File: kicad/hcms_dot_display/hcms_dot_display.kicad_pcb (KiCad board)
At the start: 2 copper layers, 35.5 x 39.9 mm, 45 parts, among them J1 Conn_01x12, J2 USB_C_Receptacle_USB2.0, J3 Conn_01x12, J4 Conn_01x10_Female, J5 Conn_01x10_Male, J6 Conn_01x10_Male, J7 Conn_01x10_Female, Q1 Q_PMOS_DSG, Q2 Q_PMOS_DSG, Q3 Q_PMOS_DSG, Q4 Q_PMOS_DSG, Q5 Q_PMOS_DSG, Q6 Q_PMOS_DSG, SW2 SW_SPST, U1 ATtiny826-SXX, U2 FT231XS

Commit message: beginning of ecos
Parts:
- added R16: DNP, Resistor_SMD:R_0603_1608Metric, F.Cu at (202.3, 120.5)
- added R17: DNP, Resistor_SMD:R_0603_1608Metric, F.Cu at (206.4, 120.5)
- C1, C2, C7, C8, C9, R15, U2: moved to F.Cu
- C12, Q6, R3, U1: moved to B.Cu
- J1, J3: footprint hcms:input board to board con top bot -> hcms:board to board con top bot
- J4: value Conn_01x10_Female -> Conn_01x11_Female; footprint Connector_PinHeader_2.54mm:PinHeader_1x10_P2.54mm_Vertical -> Connector_PinSocket_2.54mm:PinSocket_1x11_P2.54mm_Vertical
- J5: value Conn_01x10_Male -> Conn_01x11_Male; footprint Connector_PinHeader_2.54mm:PinHeader_1x10_P2.54mm_Vertical -> Connector_PinHeader_2.54mm:PinHeader_1x11_P2.54mm_Vertical
- J6: value Conn_01x10_Male -> Conn_01x12; footprint Connector_PinHeader_2.54mm:PinHeader_1x10_P2.54mm_Vertical -> hcms:board to board con left right
- J7: value Conn_01x10_Female -> Conn_01x12; footprint Connector_PinHeader_2.54mm:PinHeader_1x10_P2.54mm_Vertical -> hcms:board to board con left right
- moved J7 46.7 mm to (164.1, 99.6)
- moved Q6 42.6 mm to (180.9, 122.8), turned to -90 degrees
- moved C12 36.9 mm to (175.6, 121.0), turned to 180 degrees
- moved R3 36.7 mm to (182.4, 117.0), turned to 180 degrees
- moved U1 33.0 mm to (191.2, 123.0), turned to -90 degrees
- moved J5 25.8 mm to (167.8, 114.3), turned to 90 degrees
- moved R2 20.3 mm to (189.8, 99.8)
- moved R1 20.3 mm to (191.4, 99.8)
- moved J6 20.0 mm to (196.9, 99.6)
- moved J3 18.6 mm to (180.5, 108.3)
- moved J1 18.5 mm to (180.5, 91.2)
- moved SW2 14.7 mm to (193.3, 123.9)
- moved R6 14.4 mm to (181.3, 99.8)
- moved R7 14.4 mm to (179.8, 99.8)
- moved C2 10.2 mm to (186.1, 122.3), turned to 0 degrees
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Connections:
- J3 pad 10: /DAISY_A_DATA -> /A_DATA
- J3 pad 11: /DAISY_B_DATA -> /B_DATA
- J4 pad 10: GND -> /MCU_DATA
- J4 pad 2: /MCU_COL_1 -> /V_COL
- J4 pad 3: /MCU_COL_2 -> /MCU_COL_1
- J4 pad 4: /MCU_COL_3 -> /MCU_COL_2
- J4 pad 5: /MCU_COL_4 -> /MCU_COL_3
- J4 pad 6: /MCU_COL_5 -> /MCU_COL_4
- J4 pad 7: /nBLNK -> /MCU_COL_5
- J4 pad 8: /CLK -> /nBLNK
- J4 pad 9: /MCU_DATA -> /CLK
- J5 pad 10: GND -> /MCU_DATA
- J5 pad 2: /MCU_COL_1 -> /V_COL
- J5 pad 3: /MCU_COL_2 -> /MCU_COL_1
- J5 pad 4: /MCU_COL_3 -> /MCU_COL_2
- J5 pad 5: /MCU_COL_4 -> /MCU_COL_3
- J5 pad 6: /MCU_COL_5 -> /MCU_COL_4
- J5 pad 7: /nBLNK -> /MCU_COL_5
- J5 pad 8: /CLK -> /nBLNK
- J5 pad 9: /MCU_DATA -> /CLK
- J6 pad 10: GND -> /DAISY_A_DATA
- J6 pad 2: /MCU_COL_1 -> /V_COL
- J6 pad 3: /MCU_COL_2 -> /MCU_COL_1
- J6 pad 4: /MCU_COL_3 -> /MCU_COL_2
- J6 pad 5: /MCU_COL_4 -> /MCU_COL_3
- J6 pad 6: /MCU_COL_5 -> /MCU_COL_4
- J6 pad 7: /nBLNK -> /MCU_COL_5
- J6 pad 8: /CLK -> /nBLNK
- J6 pad 9: /MCU_DATA -> /CLK
- J7 pad 10: GND -> /A_DATA
- J7 pad 2: /MCU_COL_1 -> /V_COL
- J7 pad 3: /MCU_COL_2 -> /MCU_COL_1
- J7 pad 4: /MCU_COL_3 -> /MCU_COL_2
- J7 pad 5: /MCU_COL_4 -> /MCU_COL_3
- J7 pad 6: /MCU_COL_5 -> /MCU_COL_4
- J7 pad 7: /nBLNK -> /MCU_COL_5
- J7 pad 8: /CLK -> /nBLNK
- J7 pad 9: /MCU_DATA -> /CLK

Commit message: aidan im pushing
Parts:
- R16, R17: moved to B.Cu
- moved R17 37.7 mm to (176.9, 97.0), turned to 180 degrees
- moved R16 28.2 mm to (187.0, 97.0)
- moved C10 6.89 mm to (167.3, 97.1)

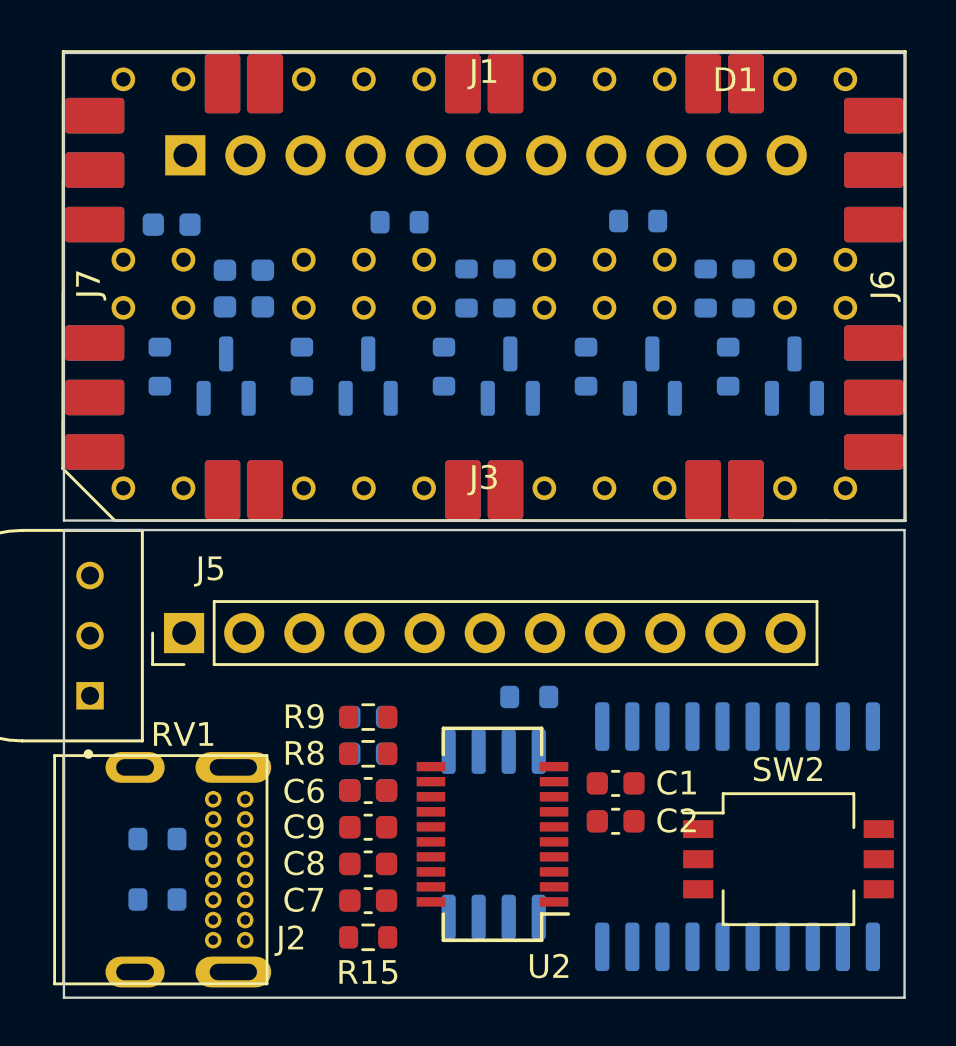
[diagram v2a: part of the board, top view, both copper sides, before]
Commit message: added switch fp, cleaned up placement. ready for routing
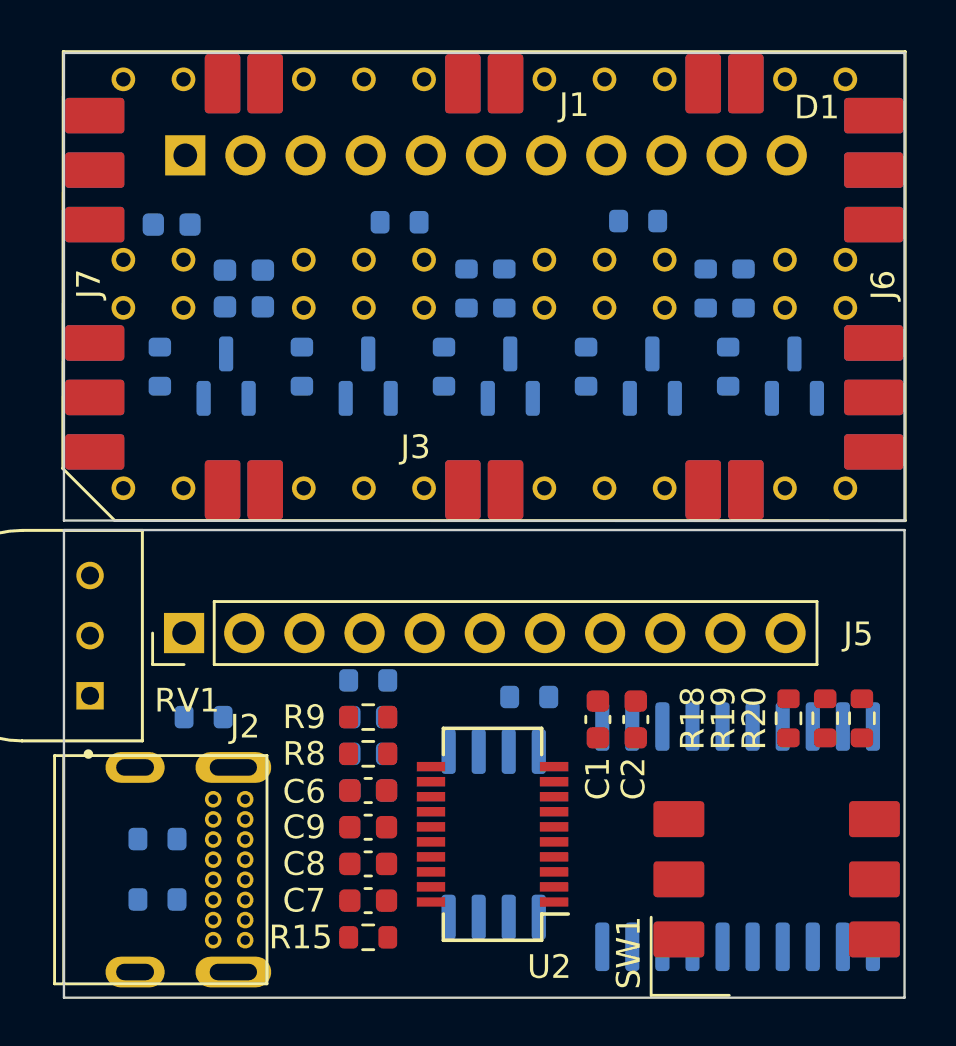
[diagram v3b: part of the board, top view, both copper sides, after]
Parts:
- removed SW2: SW_SPST, Button_Switch_SMD:SW_DIP_SPSTx03_Slide_KingTek_DSHP03TS_W7.62mm_P1.27mm
- added R18: 10k, Resistor_SMD:R_0603_1608Metric, F.Cu at (193.3, 118.0)
- added R19: 10k, Resistor_SMD:R_0603_1608Metric, F.Cu at (194.9, 118.0)
- added R20: 10k, Resistor_SMD:R_0603_1608Metric, F.Cu at (196.4, 118.0)
- added R21: 0, Resistor_SMD:R_0603_1608Metric, B.Cu at (168.7, 117.9)
- added R22: 0, Resistor_SMD:R_0603_1608Metric, B.Cu at (175.6, 116.3)
- added SW1: SW_DIP_x03, hcms:BPA03SB, F.Cu at (192.8, 124.8)
- R4, R5: value 10k -> 5.1k
- moved C2 4.38 mm to (186.9, 118.0), turned to 90 degrees
- moved C1 2.80 mm to (185.3, 118.0), turned to 90 degrees
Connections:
- C12 pad 1: /V_COL -> Net-(C12-Pad1)
- Q6 pad 1: /V_COL -> Net-(C12-Pad1)
- U1 pad 17: unconnected-(U1-Pad17) -> /CONFIG_0
- U1 pad 2: unconnected-(U1-Pad2) -> /CONFIG_1
- U1 pad 4: unconnected-(U1-Pad4) -> /CONFIG_2

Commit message: finally gonna start routing ??
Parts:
- moved C10 0.18 mm to (167.2, 97.0)
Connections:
- J4 pad 3: /MCU_COL_1 -> /MCU_COL_2
- J4 pad 4: /MCU_COL_2 -> /MCU_COL_4
- J4 pad 5: /MCU_COL_3 -> /MCU_COL_1
- J4 pad 6: /MCU_COL_4 -> /MCU_COL_3
- J5 pad 3: /MCU_COL_1 -> /MCU_COL_2
- J5 pad 4: /MCU_COL_2 -> /MCU_COL_4
- J5 pad 5: /MCU_COL_3 -> /MCU_COL_1
- J5 pad 6: /MCU_COL_4 -> /MCU_COL_3
- Q6 pad 1: Net-(C12-Pad1) -> +5V
- Q6 pad 3: Net-(Q6-Pad3) -> +5V
- Q6 pad 4: (no net) -> Net-(Q6-Pad4)
- Q6 pad 5: (no net) -> Net-(C12-Pad1)
- Q6 pad 6: (no net) -> Net-(C12-Pad1)
- Q6 pad 7: (no net) -> Net-(C12-Pad1)
- Q6 pad 8: (no net) -> Net-(C12-Pad1)
- R3 pad 2: Net-(Q6-Pad3) -> Net-(Q6-Pad4)
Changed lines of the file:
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@@
   (net 11 "/CLK")
   (net 12 "GND")
-  (net 13 "Net-(Q6-Pad3)")
+  (net 13 "Net-(Q6-Pad4)")
   (net 14 "+5V")
   (net 15 "Net-(J2-PadA5)")
@@
       (net 10 "/nBLNK") (pinfunction "nVB_13-16") (pintype "input"))
     (pad "15B" thru_hole circle locked (at 12.7 -8.635) (size 1 1) (drill 0.61) (layers *.Cu *.Mask)
-      (net 10 "/nBLNK") (pinfunction "nVB_13-16") (pintype "input"))
+      (net 10 "/nBLNK") (pinfunction "nVB_5-8") (pintype "input"))
     (pad "17A" thru_hole circle locked (at 7.62 1.015) (size 1 1) (drill 0.61) (layers *.Cu *.Mask)
       (net 11 "/CLK") (pinfunction "CLK") (pintype "input"))
@@
       (net 10 "/nBLNK") (pinfunction "nVB_9-12") (pintype "input"))
     (pad "22B" thru_hole circle locked (at -5.08 -8.635) (size 1 1) (drill 0.61) (layers *.Cu *.Mask)
-      (net 10 "/nBLNK") (pinfunction "nVB_9-12") (pintype "input"))
+      (net 10 "/nBLNK") (pinfunction "nVB_1-4") (pintype "input"))
     (pad "23A" thru_hole circle locked (at -7.62 1.015) (size 1 1) (drill 0.61) (layers *.Cu *.Mask)
       (net 14 "+5V") (pinfunction "VDD") (pintype "power_in"))
@@
       (net 6 "/V_COL") (pinfunction "Pin_2") (pintype "passive"))
     (pad "3" thru_hole oval locked (at 0 5.08 90) (size 1.7 1.7) (drill 1) (layers *.Cu *.Mask)
-      (net 28 "/MCU_COL_1") (pinfunction "Pin_3") (pintype "passive"))
+      (net 29 "/MCU_COL_2") (pinfunction "Pin_3") (pintype "passive"))
     (pad "4" thru_hole oval locked (at 0 7.62 90) (size 1.7 1.7) (drill 1) (layers *.Cu *.Mask)
-      (net 29 "/MCU_COL_2") (pinfunction "Pin_4") (pintype "passive"))
+      (net 21 "/MCU_COL_4") (pinfunction "Pin_4") (pintype "passive"))
     (pad "5" thru_hole oval locked (at 0 10.16 90) (size 1.7 1.7) (drill 1) (layers *.Cu *.Mask)
-      (net 30 "/MCU_COL_3") (pinfunction "Pin_5") (pintype "passive"))
+      (net 28 "/MCU_COL_1") (pinfunction "Pin_5") (pintype "passive"))
     (pad "6" thru_hole oval locked (at 0 12.7 90) (size 1.7 1.7) (drill 1) (layers *.Cu *.Mask)
-      (net 21 "/MCU_COL_4") (pinfunction "Pin_6") (pintype "passive"))
+      (net 30 "/MCU_COL_3") (pinfunction "Pin_6") (pintype "passive"))
     (pad "7" thru_hole oval locked (at 0 15.24 90) (size 1.7 1.7) (drill 1) (layers *.Cu *.Mask)
       (net 22 "/MCU_COL_5") (pinfunction "Pin_7") (pintype "passive"))
@@
       (net 6 "/V_COL") (pinfunction "Pin_2") (pintype "passive"))
     (pad "3" thru_hole oval locked (at 0 -5.08 270) (size 1.7 1.7) (drill 1) (layers *.Cu *.Mask)
-      (net 28 "/MCU_COL_1") (pinfunction "Pin_3") (pintype "passive"))
+      (net 29 "/MCU_COL_2") (pinfunction "Pin_3") (pintype "passive"))
     (pad "4" thru_hole oval locked (at 0 -7.62 270) (size 1.7 1.7) (drill 1) (layers *.Cu *.Mask)
-      (net 29 "/MCU_COL_2") (pinfunction "Pin_4") (pintype "passive"))
+      (net 21 "/MCU_COL_4") (pinfunction "Pin_4") (pintype "passive"))
     (pad "5" thru_hole oval locked (at 0 -10.16 270) (size 1.7 1.7) (drill 1) (layers *.Cu *.Mask)
-      (net 30 "/MCU_COL_3") (pinfunction "Pin_5") (pintype "passive"))
+      (net 28 "/MCU_COL_1") (pinfunction "Pin_5") (pintype "passive"))
     (pad "6" thru_hole oval locked (at 0 -12.7 270) (size 1.7 1.7) (drill 1) (layers *.Cu *.Mask)
-      (net 21 "/MCU_COL_4") (pinfunction "Pin_6") (pintype "passive"))
+      (net 30 "/MCU_COL_3") (pinfunction "Pin_6") (pintype "passive"))
     (pad "7" thru_hole oval locked (at 0 -15.24 270) (size 1.7 1.7) (drill 1) (layers *.Cu *.Mask)
       (net 22 "/MCU_COL_5") (pinfunction "Pin_7") (pintype "passive"))
@@
   )
   (footprint "Capacitor_SMD:C_0603_1608Metric" (layer "B.Cu")
-    (at 167.3 97.1 180)
+    (at 167.2 96.95 180)
     (descr "Capacitor SMD 0603 (1608 Metric), square (rectangular) end terminal, IPC_7351 nominal, (Body size source: IPC-SM-782 page 76, https://www.pcb-3d.com/wordpress/wp-content/uploads/ipc-sm-782a_amendment_1_and_2.pdf), generated with kicad-footprint-generator")
     (tags "capacitor")
@@
     (property "Sheetname" "")
     (attr smd)
-    (fp_text reference "C10" (at 3.4 0.05) (layer "B.SilkS")
+    (fp_text reference "C10" (at 0.65 -2.35 90) (layer "B.SilkS")
       (effects (font (size 1 1) (thickness 0.15)) (justify mirror))
     )
@@
     (fp_line (start 1.92 -1.7) (end 1.92 1.7) (layer "B.CrtYd") (width 0.05))
     (fp_line (start -1.92 -1.7) (end 1.92 -1.7) (layer "B.CrtYd") (width 0.05))
+    (fp_line (start 0.65 1.45) (end 0.65 -1.45) (layer "B.Fab") (width 0.1))
     (fp_line (start 0.65 -1.45) (end -0.65 -1.45) (layer "B.Fab") (width 0.1))
     (fp_line (start -0.65 1.125) (end -0.325 1.45) (layer "B.Fab") (width 0.1))
     (fp_line (start -0.325 1.45) (end 0.65 1.45) (layer "B.Fab") (width 0.1))
     (fp_line (start -0.65 -1.45) (end -0.65 1.125) (layer "B.Fab") (width 0.1))
-    (fp_line (start 0.65 1.45) (end 0.65 -1.45) (layer "B.Fab") (width 0.1))
     (pad "1" smd roundrect (at -0.9375 0.95 90) (size 1.475 0.6) (layers "B.Cu" "B.Paste" "B.Mask") (roundrect_rratio 0.25)
       (net 2 "/COL_2") (pinfunction "D") (pintype "passive"))
@@
       (net 66 "/COL_PWM") (pintype "passive"))
     (pad "2" smd roundrect (at 0.825 0 180) (size 0.8 0.95) (layers "B.Cu" "B.Paste" "B.Mask") (roundrect_rratio 0.25)
-      (net 13 "Net-(Q6-Pad3)") (pintype "passive"))
+      (net 13 "Net-(Q6-Pad4)") (pintype "passive"))
     (model "${KICAD6_3DMODEL_DIR}/Resistor_SMD.3dshapes/R_0603_1608Metric.wrl"
       (offset (xyz 0 0 0))
@@
     (fp_line (start 2.65 3.1) (end 2.65 -3.1) (layer "B.Fab") (width 0.1))
     (pad "1" smd roundrect (at -3.5 1.905 270) (size 1.9 0.6) (layers "B.Cu" "B.Paste" "B.Mask") (roundrect_rratio 0.25)
-      (net 67 "Net-(C12-Pad1)") (pinfunction "D") (pintype "passive"))
+      (net 14 "+5V") (pinfunction "S") (pintype "passive"))
     (pad "2" smd roundrect (at -3.5 0.635 270) (size 1.9 0.6) (layers "B.Cu" "B.Paste" "B.Mask") (roundrect_rratio 0.25)
       (net 14 "+5V") (pinfunction "S") (pintype "passive"))
     (pad "3" smd roundrect (at -3.5 -0.635 270) (size 1.9 0.6) (layers "B.Cu" "B.Paste" "B.Mask") (roundrect_rratio 0.25)
-      (net 13 "Net-(Q6-Pad3)") (pinfunction "G") (pintype "input"))
-    (pad "4" smd roundrect (at -3.5 -1.905 270) (size 1.9 0.6) (layers "B.Cu" "B.Paste" "B.Mask") (roundrect_rratio 0.25))
-    (pad "5" smd roundrect (at 3.5 -1.905 270) (size 1.9 0.6) (layers "B.Cu" "B.Paste" "B.Mask") (roundrect_rratio 0.25))
-    (pad "6" smd roundrect (at 3.5 -0.635 270) (size 1.9 0.6) (layers "B.Cu" "B.Paste" "B.Mask") (roundrect_rratio 0.25))
-    (pad "7" smd roundrect (at 3.5 0.635 270) (size 1.9 0.6) (layers "B.Cu" "B.Paste" "B.Mask") (roundrect_rratio 0.25))
-    (pad "8" smd roundrect (at 3.5 1.905 270) (size 1.9 0.6) (layers "B.Cu" "B.Paste" "B.Mask") (roundrect_rratio 0.25))
+      (net 14 "+5V") (pinfunction "S") (pintype "passive"))
+    (pad "4" smd roundrect (at -3.5 -1.905 270) (size 1.9 0.6) (layers "B.Cu" "B.Paste" "B.Mask") (roundrect_rratio 0.25)
+      (net 13 "Net-(Q6-Pad4)") (pinfunction "G") (pintype "passive"))
+    (pad "5" smd roundrect (at 3.5 -1.905 270) (size 1.9 0.6) (layers "B.Cu" "B.Paste" "B.Mask") (roundrect_rratio 0.25)
+      (net 67 "Net-(C12-Pad1)") (pinfunction "D") (pintype "passive"))
+    (pad "6" smd roundrect (at 3.5 -0.635 270) (size 1.9 0.6) (layers "B.Cu" "B.Paste" "B.Mask") (roundrect_rratio 0.25)
+      (net 67 "Net-(C12-Pad1)") (pinfunction "D") (pintype "passive"))
+    (pad "7" smd roundrect (at 3.5 0.635 270) (size 1.9 0.6) (layers "B.Cu" "B.Paste" "B.Mask") (roundrect_rratio 0.25)
+      (net 67 "Net-(C12-Pad1)") (pinfunction "D") (pintype "passive"))
+    (pad "8" smd roundrect (at 3.5 1.905 270) (size 1.9 0.6) (layers "B.Cu" "B.Paste" "B.Mask") (roundrect_rratio 0.25)
+      (net 67 "Net-(C12-Pad1)") (pinfunction "D") (pintype "passive"))
     (model "${KICAD6_3DMODEL_DIR}/Package_SO.3dshapes/SO-8_5.3x6.2mm_P1.27mm.wrl"
       (offset (xyz 0 0 0))
